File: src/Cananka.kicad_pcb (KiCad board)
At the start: 2 copper layers, 105.8 x 26 mm, 55 parts, among them J1 USB4085 B1HSW6, J2 MC 1,5/4, Q1 DMP3085, Q2 BSS84, U1 FT230XS, U2 PIC18F25K80, U3 ISO1050, U4 74LVC1T45, Y1 12 MHz

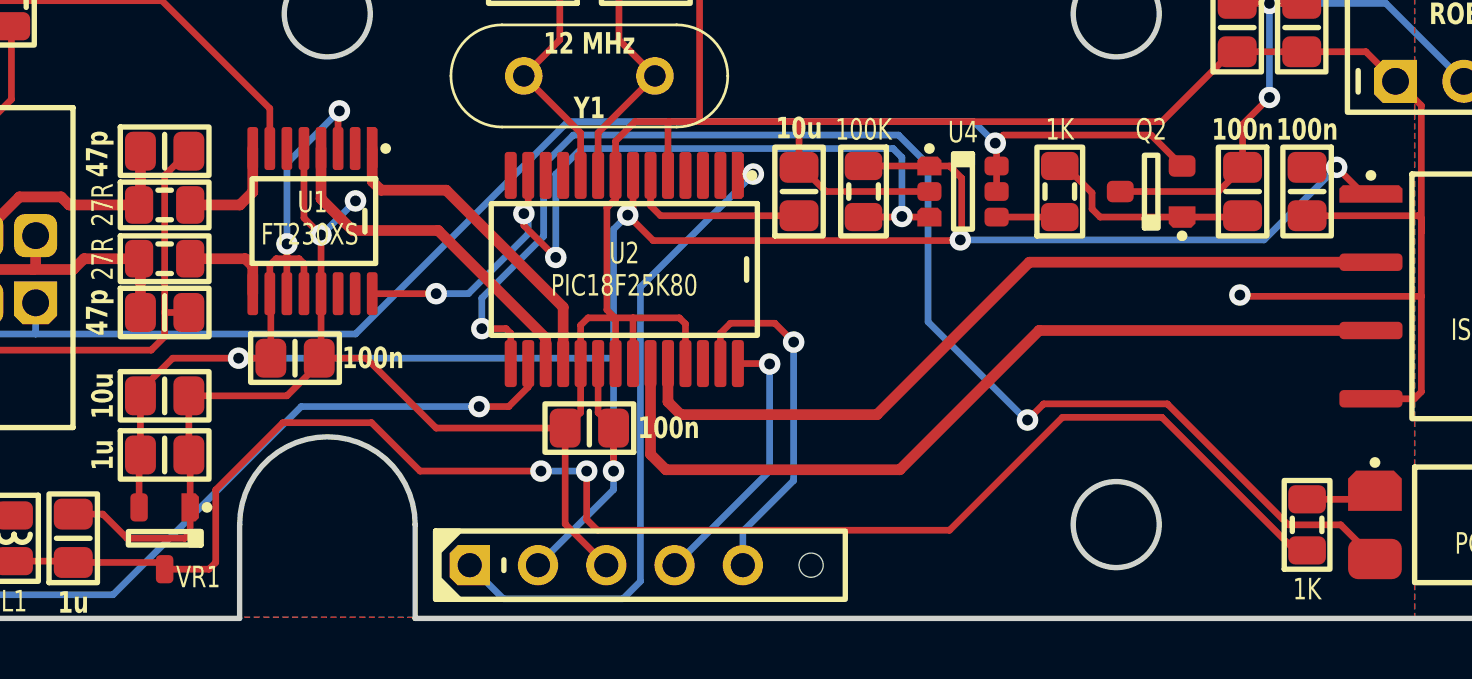
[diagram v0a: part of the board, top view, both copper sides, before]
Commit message: Moving optocoupler to 3V3 line
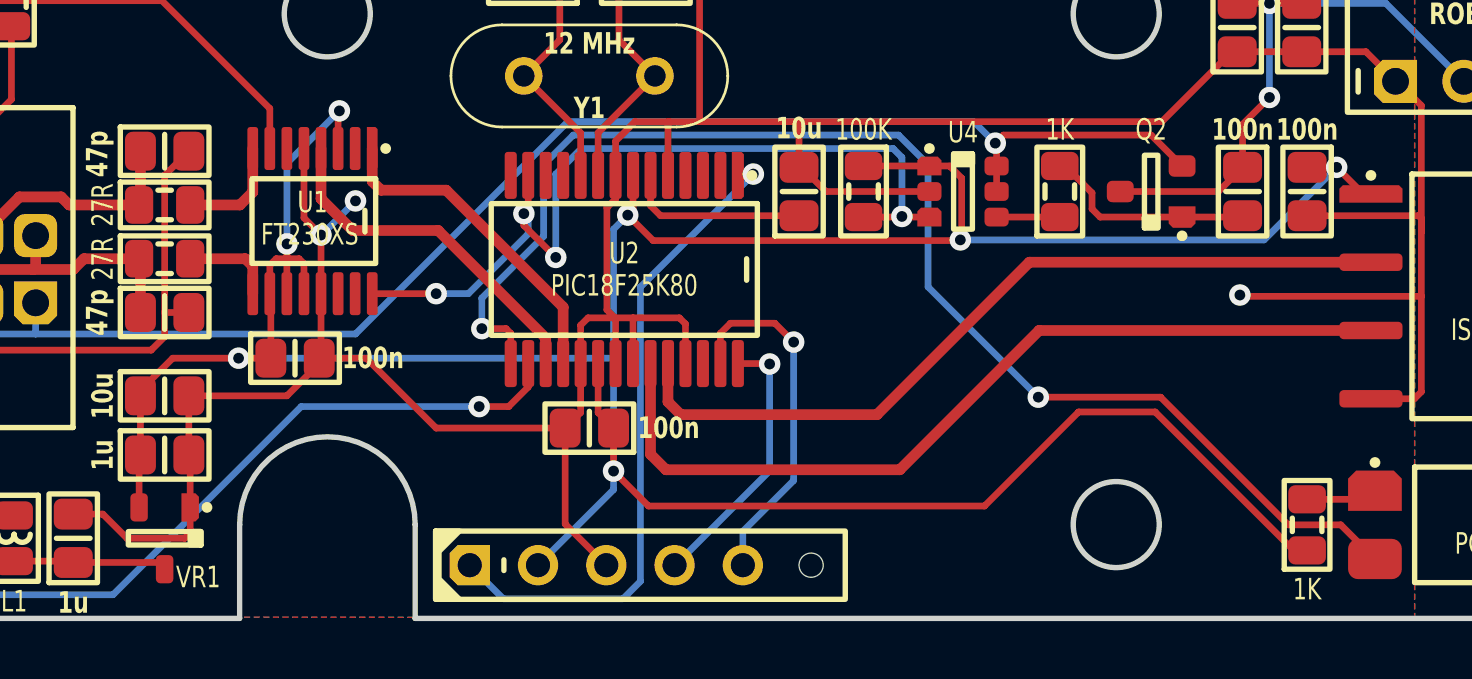
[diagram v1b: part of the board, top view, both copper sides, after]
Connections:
- R13 pad 1: A_5V -> A_3V3
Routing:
- net A_5V: track 94.6 -> 42.2 mm, vias 4 -> 2
- net A_3V3: track 95.1 -> 125.0 mm
- net A_IO_TERMINATE#: track 51.1 -> 49.9 mm

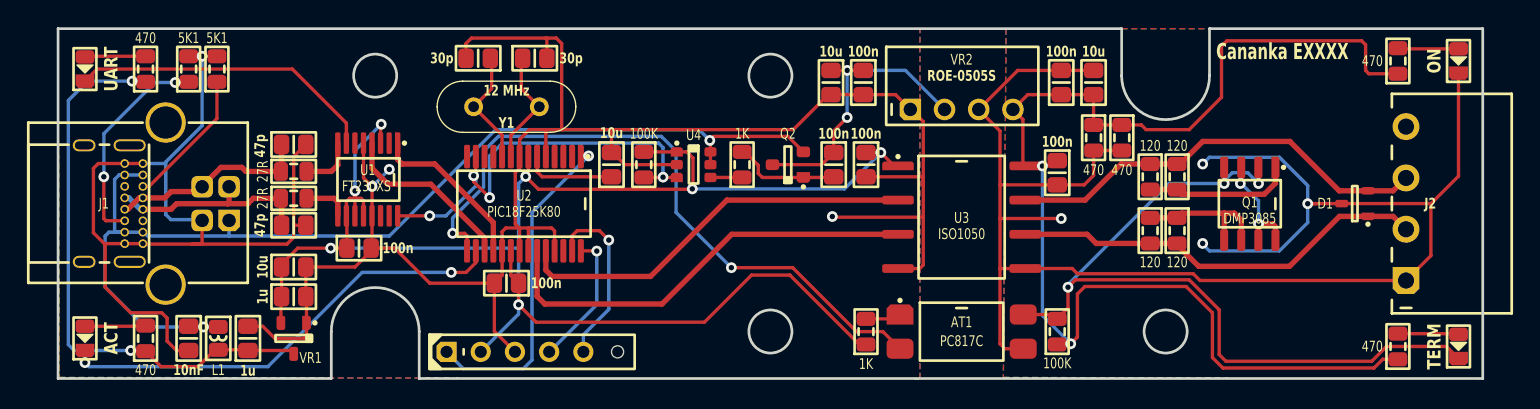
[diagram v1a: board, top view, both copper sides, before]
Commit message: Adjusted resistors a bit
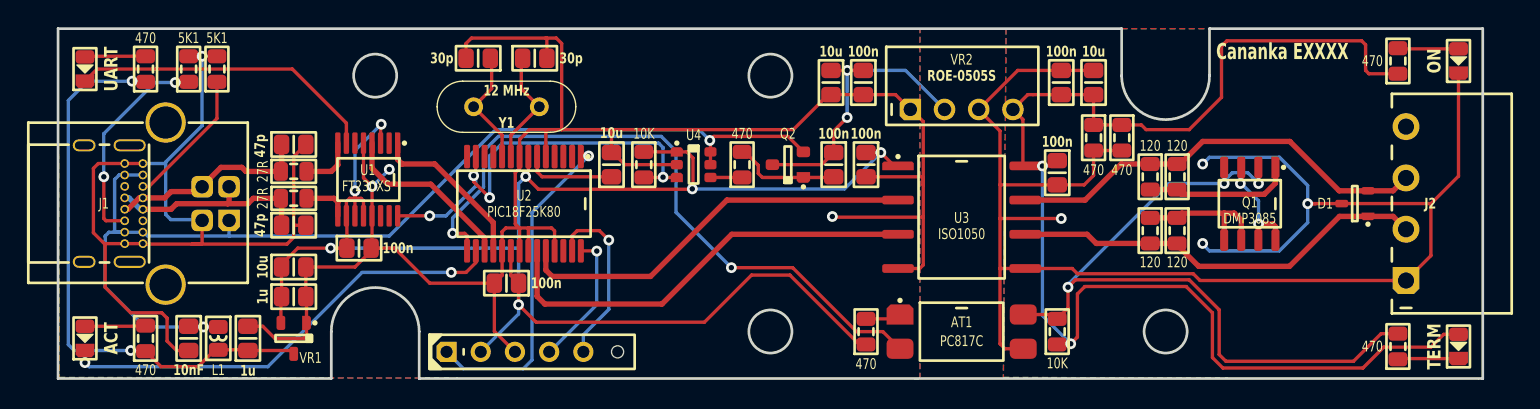
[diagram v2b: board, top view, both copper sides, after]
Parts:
- R13, R14: value 1K -> 470
- R17, R18: value 100K -> 10K
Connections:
- DS3 pad 1: B_IO_TERMINATE# -> B_LED_TERMINATE
- DS3 pad 2: B_LED_TERMINATE -> B_5V
- R12 pad 1: B_5V -> B_LED_TERMINATE
- R12 pad 2: B_LED_TERMINATE -> B_IO_TERMINATE#
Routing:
- net B_5V: track 93.1 -> 98.4 mm
- net B_IO_TERMINATE#: track 60.6 -> 56.2 mm
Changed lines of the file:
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@@
 			(layers "F.Cu" "F.Paste" "F.Mask")
 			(roundrect_rratio 0.25)
-			(net 1 "B_5V")
+			(net 26 "B_LED_TERMINATE")
 			(thermal_bridge_angle 45)
 		)
@@
 			(layers "F.Cu" "F.Paste" "F.Mask")
 			(roundrect_rratio 0.25)
-			(net 26 "B_LED_TERMINATE")
+			(net 25 "B_IO_TERMINATE#")
 			(thermal_bridge_angle 45)
 		)
@@
 			)
 		)
-		(property "Value" "1K"
+		(property "Value" "470"
 			(at 2.3 0 0)
 			(layer "F.SilkS")
@@
 			)
 		)
-		(property "Value" "100K"
+		(property "Value" "10K"
 			(at -2.35 0 0)
 			(layer "F.SilkS")
@@
 			)
 		)
-		(property "Value" "1K"
+		(property "Value" "470"
 			(at -2.4 0 0)
 			(layer "F.SilkS")
@@
 			)
 		)
-		(property "Value" "100K"
+		(property "Value" "10K"
 			(at -2.3 0 0)
 			(layer "F.SilkS")
@@
 			(chamfer_ratio 0.2)
 			(chamfer top_left bottom_left)
-			(net 25 "B_IO_TERMINATE#")
+			(net 26 "B_LED_TERMINATE")
 			(thermal_bridge_angle 45)
 		)
@@
 			(layers "F.Cu" "F.Paste" "F.Mask")
 			(roundrect_rratio 0.25)
-			(net 26 "B_LED_TERMINATE")
+			(net 1 "B_5V")
 			(thermal_bridge_angle 45)
 		)
@@
 	)
 	(segment
-		(start 96.25 39.15)
-		(end 103.775 39.15)
+		(start 122.9 42.7)
+		(end 124 42.7)
 		(width 0.25)
 		(layer "F.Cu")
@@
 	)
 	(segment
-		(start 94 43.4)
-		(end 95.2 43.4)
+		(start 121.95 43.65)
+		(end 122.9 42.7)
 		(width 0.25)
 		(layer "F.Cu")
@@
 	)
 	(segment
-		(start 105.725 41.1)
-		(end 105.725 44.425)
+		(start 94 43.4)
+		(end 95.2 43.4)
 		(width 0.25)
 		(layer "F.Cu")
@@
 	)
 	(segment
-		(start 95.7 39.7)
-		(end 96.25 39.15)
+		(start 91.65 30.19)
+		(end 93.81 30.19)
 		(width 0.25)
 		(layer "F.Cu")
@@
 	)
 	(segment
-		(start 117.725 45.2)
-		(end 118.375 44.55)
+		(start 95.7 42.9)
+		(end 95.7 39.7)
 		(width 0.25)
 		(layer "F.Cu")
@@
 	)
 	(segment
-		(start 91.65 30.19)
-		(end 93.81 30.19)
+		(start 105.725 44.425)
+		(end 106.5 45.2)
 		(width 0.25)
 		(layer "F.Cu")
@@
 	)
 	(segment
-		(start 106.5 45.2)
-		(end 117.725 45.2)
+		(start 118.45 43.65)
+		(end 121.95 43.65)
+		(width 0.25)
+		(layer "F.Cu")
+		(net 1)
+	)
+	(segment
+		(start 103.775 39.15)
+		(end 105.725 41.1)
 		(width 0.25)
 		(layer "F.Cu")
@@
 	)
 	(segment
-		(start 95.7 42.9)
-		(end 95.7 39.7)
+		(start 116.9 45.2)
+		(end 118.45 43.65)
 		(width 0.25)
 		(layer "F.Cu")
@@
 	)
 	(segment
-		(start 103.775 39.15)
-		(end 105.725 41.1)
+		(start 95.2 43.4)
+		(end 95.7 42.9)
 		(width 0.25)
 		(layer "F.Cu")
@@
 	)
 	(segment
+		(start 105.725 41.1)
+		(end 105.725 44.425)
+		(width 0.25)
+		(layer "F.Cu")
+		(net 1)
+	)
+	(segment
 		(start 106.4 25.1)
 		(end 104 27.5)
@@
 	)
 	(segment
-		(start 95.2 43.4)
-		(end 95.7 42.9)
+		(start 94.5 24.9)
+		(end 92.4 24.9)
 		(width 0.25)
 		(layer "F.Cu")
@@
 	)
 	(segment
-		(start 94.5 24.9)
-		(end 92.4 24.9)
+		(start 106.5 45.2)
+		(end 116.9 45.2)
 		(width 0.25)
 		(layer "F.Cu")
@@
 	)
 	(segment
-		(start 100.8 27.5)
-		(end 100.45 27.15)
+		(start 96.25 39.15)
+		(end 103.775 39.15)
 		(width 0.25)
 		(layer "F.Cu")
@@
 	)
 	(segment
-		(start 92.01 24.9)
-		(end 90.91 26)
+		(start 100.8 27.5)
+		(end 100.45 27.15)
 		(width 0.25)
 		(layer "F.Cu")
@@
 	)
 	(segment
-		(start 105.725 44.425)
-		(end 106.5 45.2)
+		(start 92.01 24.9)
+		(end 90.91 26)
 		(width 0.25)
 		(layer "F.Cu")
@@
 	)
 	(segment
-		(start 118.375 44.55)
-		(end 119.5 44.55)
+		(start 95.7 39.7)
+		(end 96.25 39.15)
 		(width 0.25)
 		(layer "F.Cu")
@@
 	)
 	(segment
-		(start 123.1 43.6)
-		(end 124 44.5)
+		(start 95.55 38.65)
+		(end 95 39.2)
 		(width 0.25)
 		(layer "F.Cu")
@@
 	)
 	(segment
-		(start 117.55 44.7)
-		(end 118.65 43.6)
+		(start 106.225 44.2)
+		(end 106.225 40.875)
 		(width 0.25)
 		(layer "F.Cu")
@@
 	)
 	(segment
-		(start 106.225 40.875)
+		(start 106.725 44.7)
 		(end 106.225 44.2)
 		(width 0.25)
@@
 	)
 	(segment
-		(start 104 38.65)
-		(end 106.225 40.875)
+		(start 116.2 44.7)
+		(end 106.725 44.7)
 		(width 0.25)
 		(layer "F.Cu")
@@
 	)
 	(segment
-		(start 118.65 43.6)
-		(end 123.1 43.6)
+		(start 119.5 42.65)
+		(end 118.25 42.65)
 		(width 0.25)
 		(layer "F.Cu")
@@
 	)
 	(segment
-		(start 106.725 44.7)
-		(end 117.55 44.7)
-		(width 0.25)
-		(layer "F.Cu")
-		(net 25)
-	)
-	(segment
-		(start 95.55 38.65)
-		(end 104 38.65)
-		(width 0.25)
-		(layer "F.Cu")
-		(net 25)
-	)
-	(segment
-		(start 95 39.2)
+		(start 104 38.65)
 		(end 95.55 38.65)
 		(width 0.25)
@@
 	)
 	(segment
-		(start 106.225 44.2)
-		(end 106.725 44.7)
+		(start 106.225 40.875)
+		(end 104 38.65)
+		(width 0.25)
+		(layer "F.Cu")
+		(net 25)
+	)
+	(segment
+		(start 118.25 42.65)
+		(end 116.2 44.7)
 		(width 0.25)
 		(layer "F.Cu")
@@
 	)
 	(segment
-		(start 119.5 42.65)
-		(end 123.95 42.65)
+		(start 119.55 44.5)
+		(end 119.5 44.55)
+		(width 0.25)
+		(layer "F.Cu")
+		(net 26)
+	)
+	(segment
+		(start 124 44.5)
+		(end 119.55 44.5)
 		(width 0.25)
 		(layer "F.Cu")
